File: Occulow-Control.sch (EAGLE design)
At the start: 23 parts, among them J1 CORTEX_DEBUG_PTH, T1 DMP3010LK3, T2 DMP3010LK3, T3 DMP3010LK3

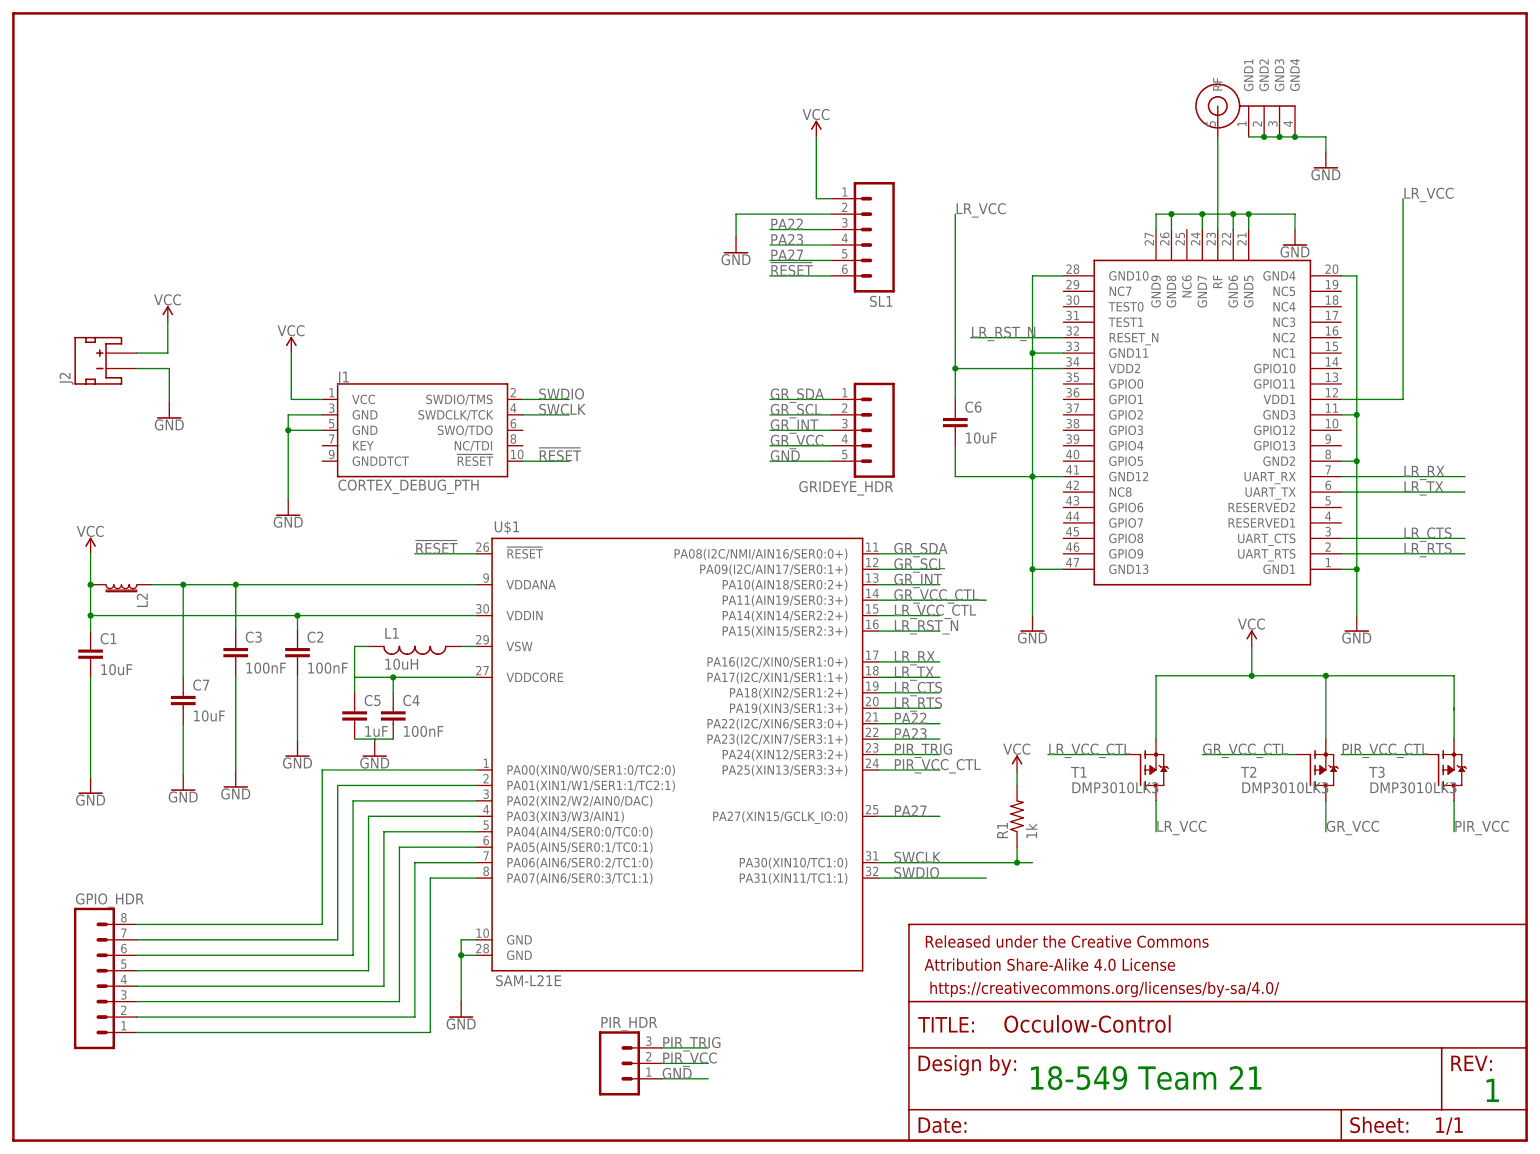
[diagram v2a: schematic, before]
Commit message: Modified assignments to ease layout
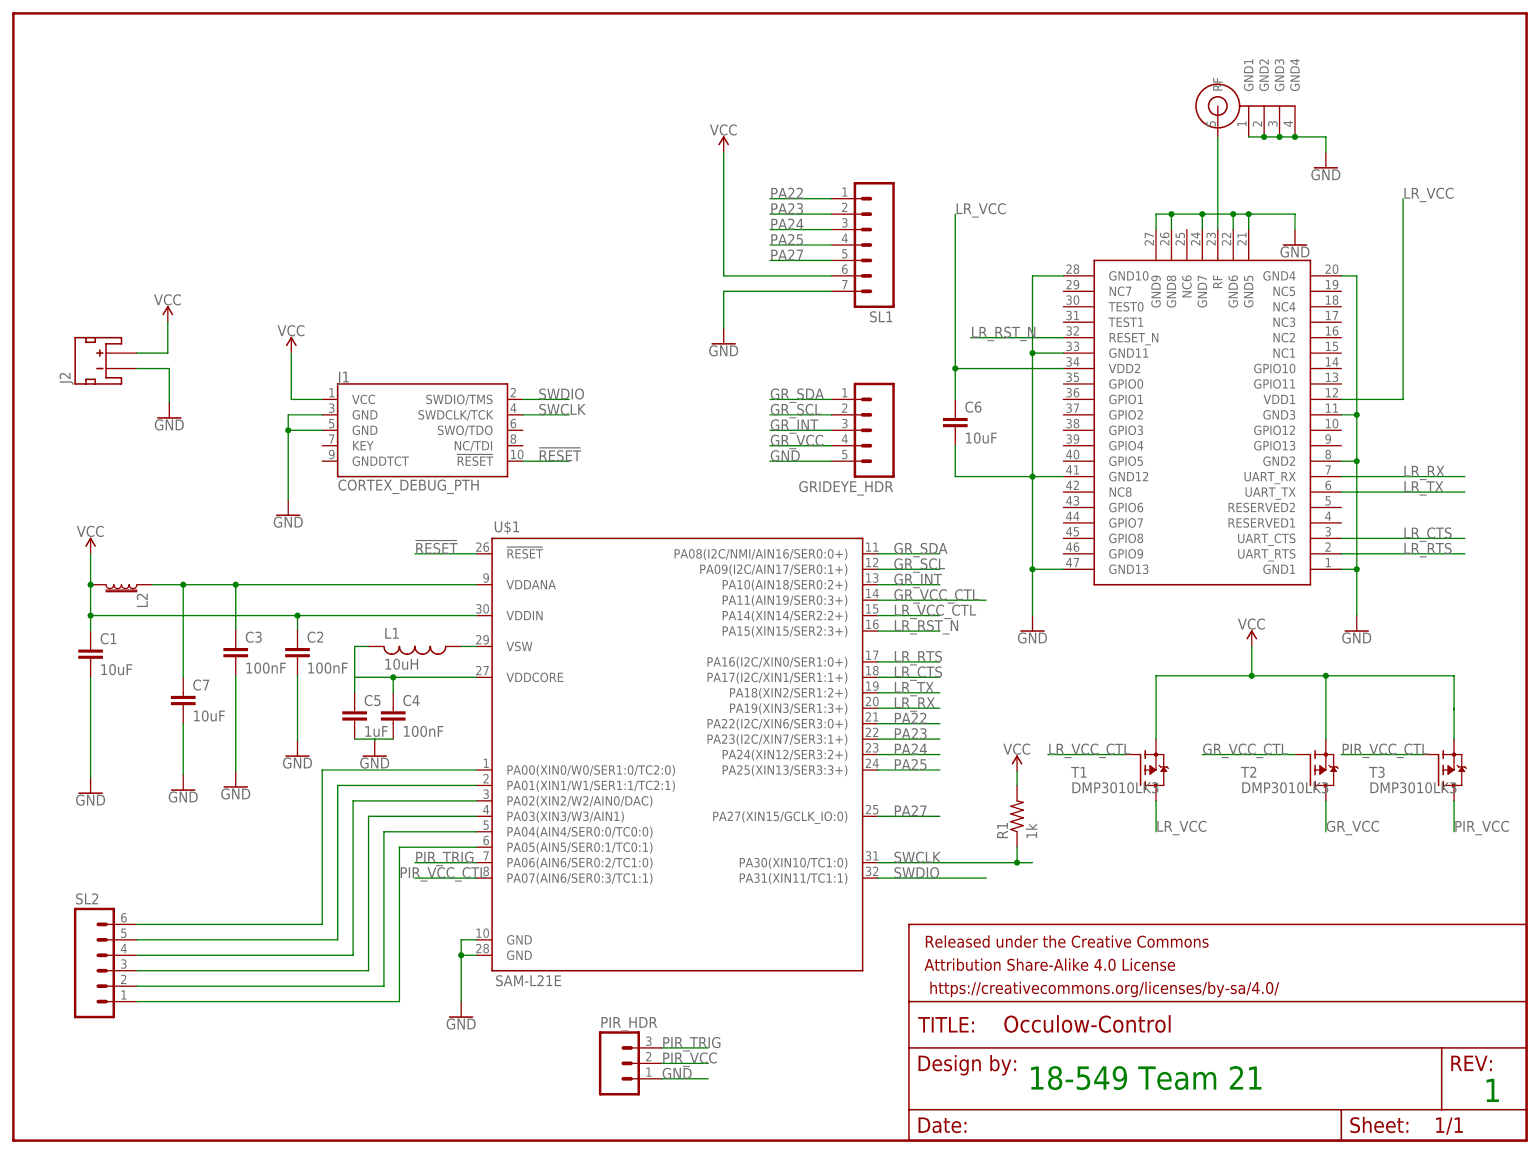
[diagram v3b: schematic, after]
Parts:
- removed GPIO_HDR: (no value), con-amp-quick:M08
- added SL2: (no value), con-amp-quick:M06
- SL1: device con-amp-quick:M06 -> con-amp-quick:M07
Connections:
- net N$1 renamed VDDCORE
- net N$10 renamed VSW
- net N$12 renamed VDDANA
- removed net N$2: GPIO_HDR.8, U$1.PA00(XIN0/W0/SER1:0/TC2:0)
- removed net N$3: GPIO_HDR.7, U$1.PA01(XIN1/W1/SER1:1/TC2:1)
- removed net N$4: GPIO_HDR.6, U$1.PA02(XIN2/W2/AIN0/DAC)
- removed net N$5: GPIO_HDR.5, U$1.PA03(XIN3/W3/AIN1)
- removed net N$6: GPIO_HDR.4, U$1.PA04(AIN4/SER0:0/TC0:0)
- removed net N$7: GPIO_HDR.3, U$1.PA05(AIN5/SER0:1/TC0:1)
- removed net N$8: GPIO_HDR.2, U$1.PA06(AIN6/SER0:2/TC1:0)
- removed net N$9: GPIO_HDR.1, U$1.PA07(AIN6/SER0:3/TC1:1)
- new net PA00: SL2.6, U$1.PA00(XIN0/W0/SER1:0/TC2:0)
- new net PA01: SL2.5, U$1.PA01(XIN1/W1/SER1:1/TC2:1)
- new net PA02: SL2.4, U$1.PA02(XIN2/W2/AIN0/DAC)
- new net PA03: SL2.3, U$1.PA03(XIN3/W3/AIN1)
- new net PA04: SL2.2, U$1.PA04(AIN4/SER0:0/TC0:0)
- new net PA05: SL2.1, U$1.PA05(AIN5/SER0:1/TC0:1)
- new net PA24: SL1.3, U$1.PA24(XIN12/SER3:2+)
- new net PA25: SL1.4, U$1.PA25(XIN13/SER3:3+)
- net !RESET: no longer SL1.6
- net GND: now also SL1.7; no longer SL1.2
- net LR_CTS: now also U$1.PA17(I2C/XIN1/SER1:1+); no longer U$1.PA18(XIN2/SER1:2+)
- net LR_RTS: now also U$1.PA16(I2C/XIN0/SER1:0+); no longer U$1.PA19(XIN3/SER1:3+)
- net LR_RX: now also U$1.PA19(XIN3/SER1:3+); no longer U$1.PA16(I2C/XIN0/SER1:0+)
- net LR_TX: now also U$1.PA18(XIN2/SER1:2+); no longer U$1.PA17(I2C/XIN1/SER1:1+)
- net PA22: now also SL1.1; no longer SL1.3
- net PA23: now also SL1.2; no longer SL1.4
- net PIR_TRIG: now also U$1.PA06(AIN6/SER0:2/TC1:0); no longer U$1.PA24(XIN12/SER3:2+)
- net PIR_VCC_CTL: now also U$1.PA07(AIN6/SER0:3/TC1:1); no longer U$1.PA25(XIN13/SER3:3+)
- net VCC: now also SL1.6; no longer SL1.1

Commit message: Standoffs
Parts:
- added H1, H2, H3, H4: STAND-OFF, SparkFun-Hardware:STAND-OFF
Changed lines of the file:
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@@
 <part name="GND13" library="SparkFun-PowerSymbols" deviceset="GND" device=""/>
 <part name="SL2" library="con-amp-quick" deviceset="M06" device=""/>
+<part name="H1" library="SparkFun-Hardware" deviceset="STAND-OFF" device=""/>
+<part name="H2" library="SparkFun-Hardware" deviceset="STAND-OFF" device=""/>
+<part name="H3" library="SparkFun-Hardware" deviceset="STAND-OFF" device=""/>
+<part name="H4" library="SparkFun-Hardware" deviceset="STAND-OFF" device=""/>
 </parts>
 <sheets>
@@
 <instance part="GND13" gate="1" x="46.736" y="63.246"/>
 <instance part="SL2" gate="G$1" x="15.24" y="27.94"/>
+<instance part="H1" gate="G$1" x="35.56" y="5.08"/>
+<instance part="H2" gate="G$1" x="40.64" y="5.08"/>
+<instance part="H3" gate="G$1" x="48.26" y="5.08"/>
+<instance part="H4" gate="G$1" x="55.88" y="5.08"/>
 </instances>
 <busses>
